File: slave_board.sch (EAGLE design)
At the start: 150 parts, among them IC3 ATMEGA2560-16AU, J1 OSTVN08A150, J11 1935161, J12 OSTVN06A150, J13 OSTVN08A150, J17 RJ45, J18 OSTVN08A150, J2 OSTVN08A150, J22 RJ45, J3 1935161, J4 OSTVN06A150, J6 1935161, J8 OSTVN08A150, K1 ORWH-SH-112D1F, Q1 PHB45NQ15T, Q2 PHB45NQ15T, Q3 BSS138L, Q5 BSS138L, Q7 PHB45NQ15T, Q8 IRFR9024TRPBF, U1 VNQ5E160KTR-E, U2 PCA9615, U3 INA213AIDCKT, U4 VNH7070ASTR, U5 VNH7070ASTR, U6 VNQ5E160KTR-E, U7 INA213AIDCKT, U8 LM340MP-5.0/NOPB, U9 LM340MP-5.0/NOPB, Y1 ABLS-16.000MHZ-B4-T

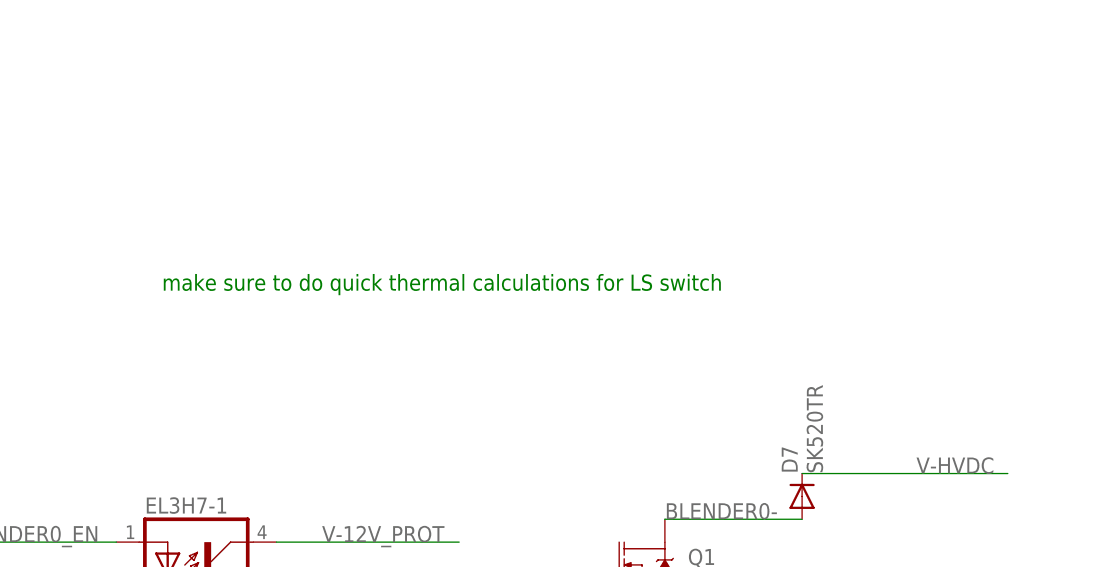
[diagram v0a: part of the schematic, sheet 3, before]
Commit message: added fuse amperage in silkscreen
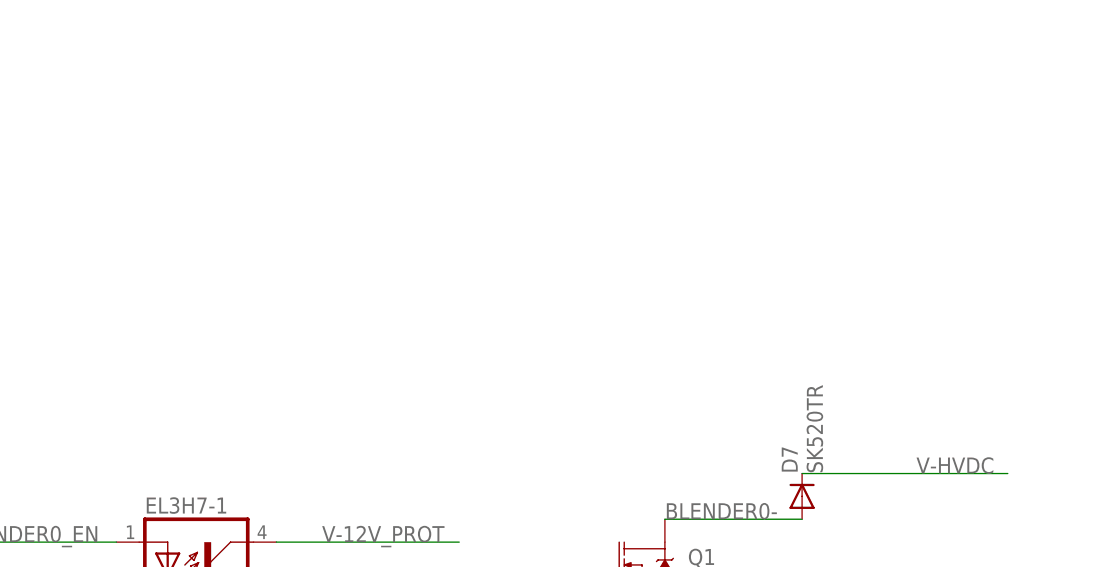
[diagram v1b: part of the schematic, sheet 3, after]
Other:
- note removed: "make sure to do quick thermal calculations for LS switch"
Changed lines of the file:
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@@
 <text x="68.58" y="246.38" size="2.54" layer="91">DC Motor Driver Uni-Direction</text>
 <text x="312.42" y="226.06" size="2.54" layer="91">Cup/Carousel Stepper Driver</text>
-<text x="231.14" y="137.16" size="1.778" layer="91">make sure to do quick thermal calculations for LS switch</text>
 <text x="276.86" y="236.22" size="1.778" layer="91">for Pololu: https://www.pololu.com/product/2133/specs (uses DRV8825PWP)
 Need heat-sinking or forced air

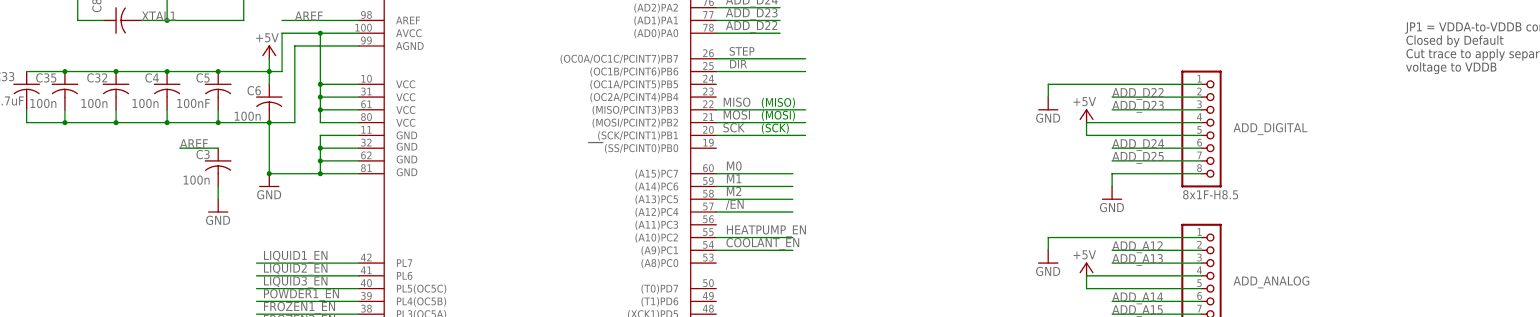
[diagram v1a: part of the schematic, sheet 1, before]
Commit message: increased blender vias to gnd, added individual blender fuses,addition aref cap, and debug leds
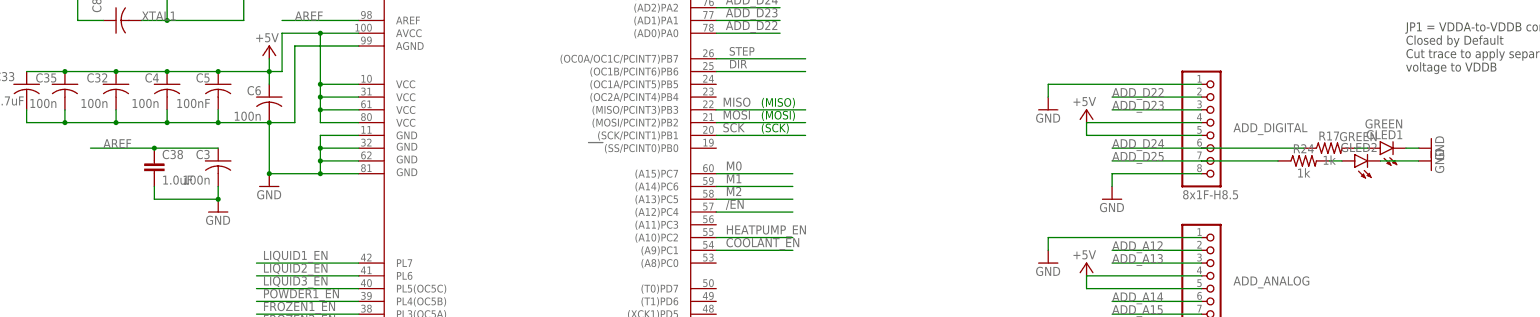
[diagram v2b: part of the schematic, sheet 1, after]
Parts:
- added C38: 1.0uF, SparkFun-Capacitors:1.0UF-0603-16V-10%
- added F2, F3: SSQ7, smoothio:SSQ7
- added GLED1, GLED2: GREEN, led:LEDCHIP-LED0805
- added R17, R24: 1k, SparkFun-Resistors:1KOHM-0603-1/10W-1%
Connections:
- new net FUSE0-: D7.C, F2.2, J24.1
- new net FUSE1-: D8.C, F3.2, J9.1
- new net N$2: GLED1.A, R17.2
- new net N$5: GLED2.A, R24.2
- net ADD_D24: now also R17.1
- net ADD_D25: now also R24.1
- net AREF: now also C38.1
- net GND: now also C38.2, GLED1.C, GLED2.C
- net V-HVDC: now also F2.1, F3.1; no longer D7.C, D8.C, J24.1, J9.1
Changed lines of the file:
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@@
 <part name="GND64" library="supply1" library_urn="urn:adsk.eagle:library:371" deviceset="GND" device=""/>
 <part name="GND66" library="supply1" library_urn="urn:adsk.eagle:library:371" deviceset="GND" device=""/>
+<part name="F2" library="smoothio" deviceset="SSQ7" device=""/>
+<part name="F3" library="smoothio" deviceset="SSQ7" device=""/>
+<part name="GLED1" library="led" library_urn="urn:adsk.eagle:library:259" deviceset="LED" device="CHIP-LED0805" package3d_urn="urn:adsk.eagle:package:15818/2" value="GREEN"/>
+<part name="GND34" library="supply1" library_urn="urn:adsk.eagle:library:371" deviceset="GND" device=""/>
+<part name="R17" library="SparkFun-Resistors" library_urn="urn:adsk.eagle:library:532" deviceset="1KOHM" device="-0603-1/10W-1%" package3d_urn="urn:adsk.eagle:package:39650/1" value="1k"/>
+<part name="GLED2" library="led" library_urn="urn:adsk.eagle:library:259" deviceset="LED" device="CHIP-LED0805" package3d_urn="urn:adsk.eagle:package:15818/2" value="GREEN"/>
+<part name="GND51" library="supply1" library_urn="urn:adsk.eagle:library:371" deviceset="GND" device=""/>
+<part name="R24" library="SparkFun-Resistors" library_urn="urn:adsk.eagle:library:532" deviceset="1KOHM" device="-0603-1/10W-1%" package3d_urn="urn:adsk.eagle:package:39650/1" value="1k"/>
+<part name="C38" library="SparkFun-Capacitors" library_urn="urn:adsk.eagle:library:510" deviceset="1.0UF" device="-0603-16V-10%" package3d_urn="urn:adsk.eagle:package:37414/1" value="1.0uF"/>
 </parts>
 <sheets>
@@
 <attribute name="VALUE" x="74.676" y="155.321" size="1.778" layer="96" rot="MR0"/>
 </instance>
+<instance part="GLED1" gate="G$1" x="337.82" y="147.32" smashed="yes" rot="R90">
+<attribute name="NAME" x="342.392" y="150.876" size="1.778" layer="95" rot="R180"/>
+<attribute name="VALUE" x="342.392" y="153.035" size="1.778" layer="96" rot="R180"/>
+</instance>
+<instance part="GND34" gate="1" x="347.98" y="147.32" smashed="yes" rot="R90">
+<attribute name="VALUE" x="350.52" y="144.78" size="1.778" layer="96" rot="R90"/>
+</instance>
+<instance part="R17" gate="G$1" x="327.66" y="147.32" smashed="yes">
+<attribute name="NAME" x="327.66" y="148.844" size="1.778" layer="95" font="vector" align="bottom-center"/>
+<attribute name="VALUE" x="327.66" y="145.796" size="1.778" layer="96" font="vector" align="top-center"/>
+</instance>
+<instance part="GLED2" gate="G$1" x="332.74" y="144.78" smashed="yes" rot="R90">
+<attribute name="NAME" x="337.312" y="148.336" size="1.778" layer="95" rot="R180"/>
+<attribute name="VALUE" x="337.312" y="150.495" size="1.778" layer="96" rot="R180"/>
+</instance>
+<instance part="GND51" gate="1" x="347.98" y="144.78" smashed="yes" rot="R90">
+<attribute name="VALUE" x="350.52" y="142.24" size="1.778" layer="96" rot="R90"/>
+</instance>
+<instance part="R24" gate="G$1" x="322.58" y="144.78" smashed="yes">
+<attribute name="NAME" x="322.58" y="146.304" size="1.778" layer="95" font="vector" align="bottom-center"/>
+<attribute name="VALUE" x="322.58" y="143.256" size="1.778" layer="96" font="vector" align="top-center"/>
+</instance>
+<instance part="C38" gate="G$1" x="93.98" y="142.24" smashed="yes">
+<attribute name="NAME" x="95.504" y="145.161" size="1.778" layer="95" font="vector"/>
+<attribute name="VALUE" x="95.504" y="140.081" size="1.778" layer="96" font="vector"/>
+</instance>
 </instances>
 <busses>
@@
 <pinref part="C3" gate="G$1" pin="2"/>
 <pinref part="GND8" gate="1" pin="GND"/>
+<pinref part="C38" gate="G$1" pin="2"/>
+<wire x1="93.98" y1="139.7" x2="93.98" y2="137.16" width="0.1524" layer="91"/>
+<wire x1="93.98" y1="137.16" x2="106.68" y2="137.16" width="0.1524" layer="91"/>
+<junction x="106.68" y="137.16"/>
 </segment>
 <segment>
@@
 <pinref part="GND82" gate="1" pin="GND"/>
 </segment>
+<segment>
+<wire x1="345.44" y1="147.32" x2="342.9" y2="147.32" width="0.1524" layer="91"/>
+<pinref part="GND34" gate="1" pin="GND"/>
+<pinref part="GLED1" gate="G$1" pin="C"/>
+</segment>
+<segment>
+<wire x1="345.44" y1="144.78" x2="337.82" y2="144.78" width="0.1524" layer="91"/>
+<pinref part="GND51" gate="1" pin="GND"/>
+<pinref part="GLED2" gate="G$1" pin="C"/>
+</segment>
 </net>
 <net name="AREF" class="0">
@@
 </segment>
 <segment>
-<wire x1="106.68" y1="147.32" x2="99.06" y2="147.32" width="0.1524" layer="91"/>
-<label x="99.06" y="147.32" size="1.778" layer="95"/>
+<wire x1="106.68" y1="147.32" x2="93.98" y2="147.32" width="0.1524" layer="91"/>
+<label x="83.82" y="147.32" size="1.778" layer="95"/>
 <pinref part="C3" gate="G$1" pin="1"/>
+<pinref part="C38" gate="G$1" pin="1"/>
+<junction x="93.98" y="147.32"/>
+<wire x1="93.98" y1="147.32" x2="81.28" y2="147.32" width="0.1524" layer="91"/>
 </segment>
 </net>
@@
 <pinref part="ADD_DIGITAL" gate="A" pin="6"/>
 <label x="284.48" y="147.32" size="1.778" layer="95"/>
+<wire x1="302.26" y1="147.32" x2="322.58" y2="147.32" width="0.1524" layer="91"/>
+<pinref part="R17" gate="G$1" pin="1"/>
 </segment>
 </net>
@@
 <pinref part="ADD_DIGITAL" gate="A" pin="7"/>
 <label x="284.48" y="144.78" size="1.778" layer="95"/>
+<wire x1="302.26" y1="144.78" x2="317.5" y2="144.78" width="0.1524" layer="91"/>
+<pinref part="R24" gate="G$1" pin="1"/>
 </segment>
 </net>
@@
 </segment>
 </net>
+<net name="N$2" class="0">
+<segment>
+<wire x1="335.28" y1="147.32" x2="332.74" y2="147.32" width="0.1524" layer="91"/>
+<pinref part="GLED1" gate="G$1" pin="A"/>
+<pinref part="R17" gate="G$1" pin="2"/>
+</segment>
+</net>
+<net name="N$5" class="0">
+<segment>
+<wire x1="330.2" y1="144.78" x2="327.66" y2="144.78" width="0.1524" layer="91"/>
+<pinref part="GLED2" gate="G$1" pin="A"/>
+<pinref part="R24" gate="G$1" pin="2"/>
+</segment>
+</net>
 </nets>
 </sheet>
@@
 </segment>
 </net>
-<net name="V-HVDC" class="4">
+<net name="FUSE0-" class="4">
 <segment>
 <pinref part="D7" gate="G$1" pin="C"/>
@@
 <label x="314.96" y="116.84" size="1.778" layer="95"/>
 </segment>
+</net>
+<net name="FUSE1-" class="4">
 <segment>
 <pinref part="D8" gate="G$1" pin="C"/>
@@
 <attribute name="VALUE" x="22.86" y="180.34" size="1.778" layer="96"/>
 </instance>
+<instance part="F2" gate="G$1" x="233.68" y="236.22" smashed="yes">
+<attribute name="NAME" x="229.87" y="237.617" size="1.778" layer="95"/>
+<attribute name="VALUE" x="229.87" y="233.299" size="1.778" layer="96"/>
+</instance>
+<instance part="F3" gate="G$1" x="233.68" y="215.9" smashed="yes">
+<attribute name="NAME" x="229.87" y="217.297" size="1.778" layer="95"/>
+<attribute name="VALUE" x="229.87" y="212.979" size="1.778" layer="96"/>
+</instance>
 </instances>
 <busses>
@@
 <net name="V-HVDC" class="4">
 <segment>
-<wire x1="226.06" y1="236.22" x2="251.46" y2="236.22" width="0.1524" layer="91"/>
-<label x="226.06" y="236.22" size="1.778" layer="95"/>
-<pinref part="J24" gate="G$1" pin="1"/>
+<pinref part="F2" gate="G$1" pin="1"/>
+<wire x1="228.6" y1="236.22" x2="218.44" y2="236.22" width="0.1524" layer="91"/>
+<label x="218.44" y="236.22" size="1.778" layer="95"/>
 </segment>
 <segment>
-<wire x1="226.06" y1="215.9" x2="251.46" y2="215.9" width="0.1524" layer="91"/>
-<label x="226.06" y="215.9" size="1.778" layer="95"/>
-<pinref part="J9" gate="G$1" pin="1"/>
+<pinref part="F3" gate="G$1" pin="1"/>
+<wire x1="228.6" y1="215.9" x2="218.44" y2="215.9" width="0.1524" layer="91"/>
+<label x="218.44" y="215.9" size="1.778" layer="95"/>
 </segment>
 </net>
@@
 </segment>
 </net>
+<net name="FUSE1-" class="4">
+<segment>
+<wire x1="238.76" y1="215.9" x2="251.46" y2="215.9" width="0.1524" layer="91"/>
+<label x="238.76" y="215.9" size="1.778" layer="95"/>
+<pinref part="J9" gate="G$1" pin="1"/>
+<pinref part="F3" gate="G$1" pin="2"/>
+</segment>
+</net>
+<net name="FUSE0-" class="4">
+<segment>
+<wire x1="238.76" y1="236.22" x2="251.46" y2="236.22" width="0.1524" layer="91"/>
+<label x="238.76" y="236.22" size="1.778" layer="95"/>
+<pinref part="J24" gate="G$1" pin="1"/>
+<pinref part="F2" gate="G$1" pin="2"/>
+</segment>
+</net>

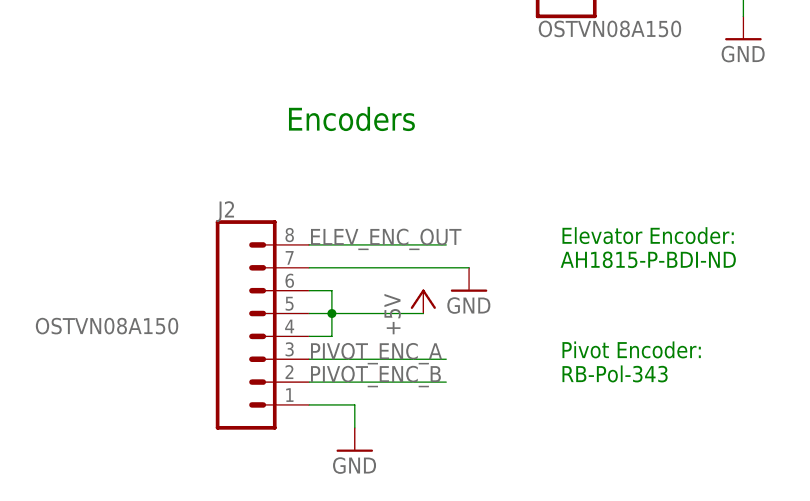
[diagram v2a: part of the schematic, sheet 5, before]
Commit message: mapped additional elevator encoder input
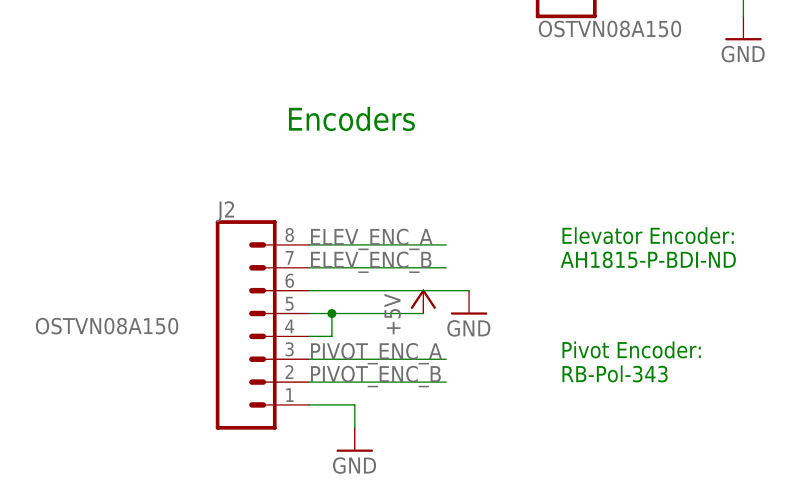
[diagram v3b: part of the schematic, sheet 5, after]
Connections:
- removed net ELEV_ENC_OUT: IC3.(TXD1/INT3)PD3, J2.8
- new net ELEV_ENC_A: IC3.(RXD1/INT2)PD2, J2.8
- new net ELEV_ENC_B: IC3.(TXD1/INT3)PD3, J2.7
- net +5V: no longer J2.6
- net GND: now also J2.6; no longer J2.7
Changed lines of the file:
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@@
-</segment>
-</net>
-<net name="ELEV_ENC_OUT" class="0">
-<segment>
-<wire x1="220.98" y1="109.22" x2="205.74" y2="109.22" width="0.1524" layer="91"/>
-<label x="207.645" y="109.855" size="1.778" layer="95"/>
-<pinref part="IC3" gate="1" pin="(TXD1/INT3)PD3"/>
 </segment>
 </net>
@@
 <pinref part="GLED2" gate="G$1" pin="A"/>
 <pinref part="R24" gate="G$1" pin="2"/>
+</segment>
+</net>
+<net name="ELEV_ENC_A" class="0">
+<segment>
+<pinref part="IC3" gate="1" pin="(RXD1/INT2)PD2"/>
+<wire x1="205.74" y1="106.68" x2="220.98" y2="106.68" width="0.1524" layer="91"/>
+<label x="205.74" y="106.68" size="1.778" layer="95"/>
+</segment>
+</net>
+<net name="ELEV_ENC_B" class="0">
+<segment>
+<wire x1="220.98" y1="109.22" x2="205.74" y2="109.22" width="0.1524" layer="91"/>
+<pinref part="IC3" gate="1" pin="(TXD1/INT3)PD3"/>
+<label x="205.74" y="109.22" size="1.778" layer="95"/>
 </segment>
 </net>
@@
 <attribute name="NAME" x="53.34" y="91.948" size="1.778" layer="95" font="vector"/>
 </instance>
-<instance part="GND59" gate="1" x="81.28" y="83.82" smashed="yes">
-<attribute name="VALUE" x="78.74" y="81.28" size="1.778" layer="96"/>
+<instance part="GND59" gate="1" x="81.28" y="81.28" smashed="yes">
+<attribute name="VALUE" x="78.74" y="78.74" size="1.778" layer="96"/>
 </instance>
 <instance part="GND63" gate="1" x="68.58" y="66.04" smashed="yes">
@@
 <pinref part="J2" gate="G$1" pin="5"/>
 <wire x1="63.5" y1="81.28" x2="66.04" y2="81.28" width="0.1524" layer="91"/>
-<pinref part="J2" gate="G$1" pin="6"/>
 <wire x1="66.04" y1="81.28" x2="76.2" y2="81.28" width="0.1524" layer="91"/>
-<wire x1="63.5" y1="83.82" x2="66.04" y2="83.82" width="0.1524" layer="91"/>
-<wire x1="66.04" y1="83.82" x2="66.04" y2="81.28" width="0.1524" layer="91"/>
 <junction x="66.04" y="81.28"/>
 <pinref part="J2" gate="G$1" pin="4"/>
@@
 </segment>
 <segment>
-<pinref part="J2" gate="G$1" pin="7"/>
+<pinref part="J2" gate="G$1" pin="6"/>
 <pinref part="GND59" gate="1" pin="GND"/>
-<wire x1="63.5" y1="86.36" x2="81.28" y2="86.36" width="0.1524" layer="91"/>
+<wire x1="63.5" y1="83.82" x2="81.28" y2="83.82" width="0.1524" layer="91"/>
 </segment>
 </net>
@@
 </segment>
 </net>
-<net name="ELEV_ENC_OUT" class="0">
+<net name="ELEV_ENC_A" class="0">
 <segment>
 <pinref part="J2" gate="G$1" pin="8"/>
@@
 </segment>
 </net>
+<net name="ELEV_ENC_B" class="0">
+<segment>
+<pinref part="J2" gate="G$1" pin="7"/>
+<wire x1="63.5" y1="86.36" x2="78.74" y2="86.36" width="0.1524" layer="91"/>
+<label x="63.5" y="86.36" size="1.778" layer="95"/>
+</segment>
+</net>
